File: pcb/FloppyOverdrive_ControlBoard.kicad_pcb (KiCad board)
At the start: 2 copper layers, 163 x 104 mm, 46 parts, among them J1 174804-1, J2 Motor_Header, J3 Bus_Connector, J4 Sensor_Header, J5 Heads_Header, J6 Step_Header, J7 PIC_ADC_Header, J8 FPGA_IO_Header, J9 HeadOut_Header, SW1 RST_Btn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

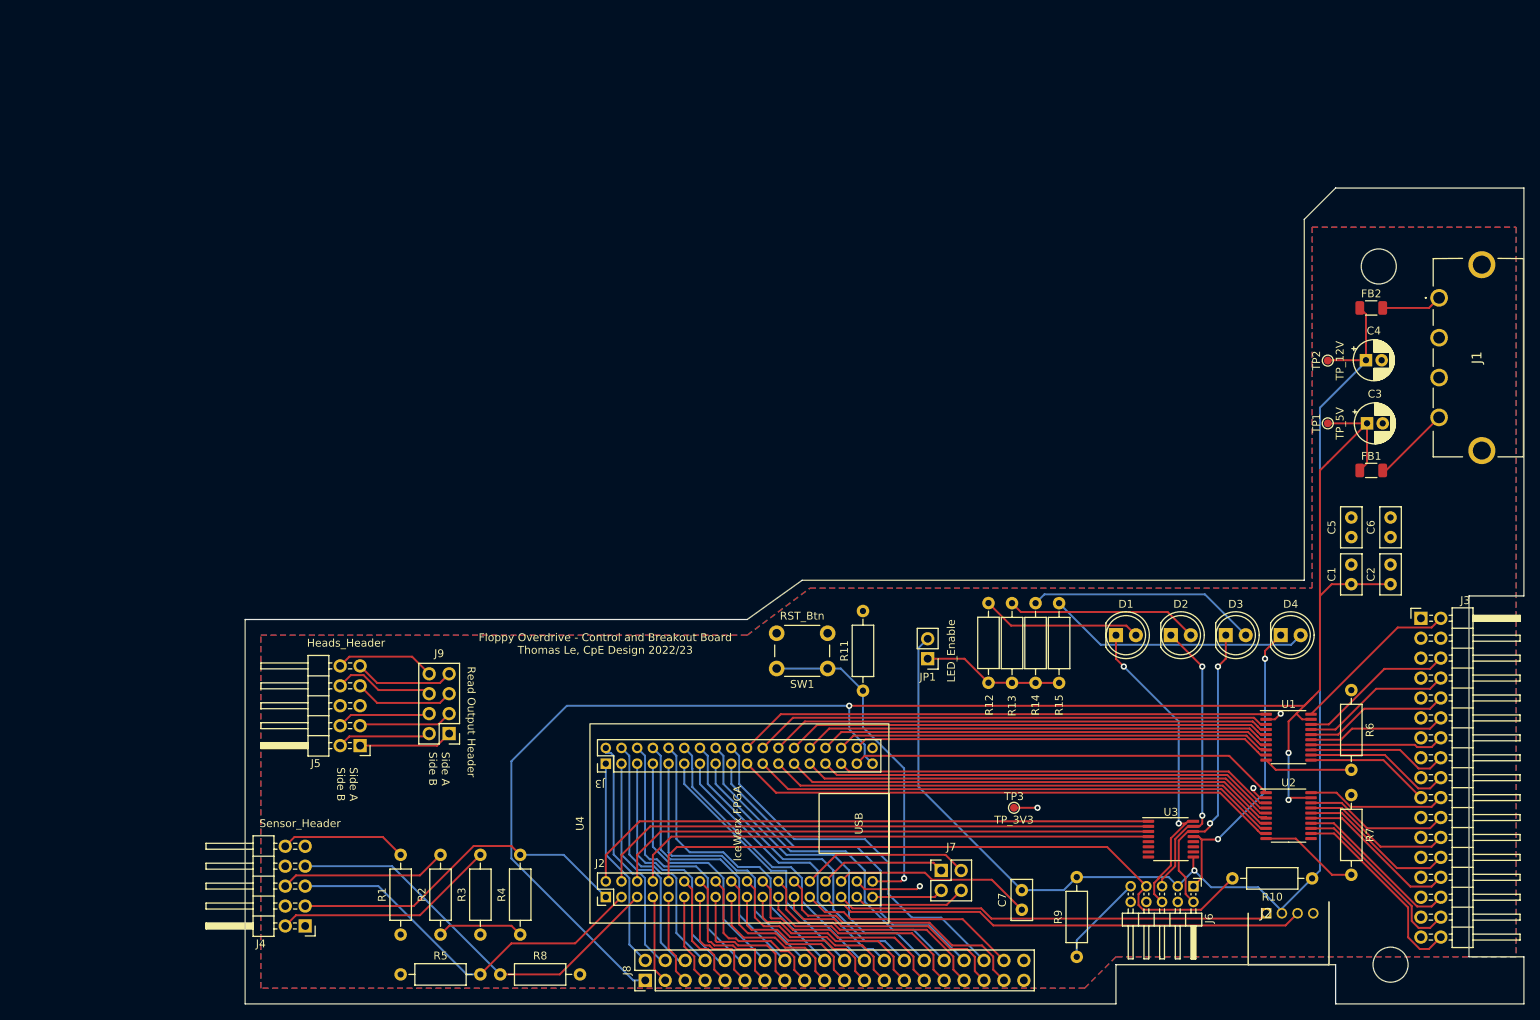
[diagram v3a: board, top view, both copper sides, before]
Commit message: Fixed incorrect routing, added silkscreen info
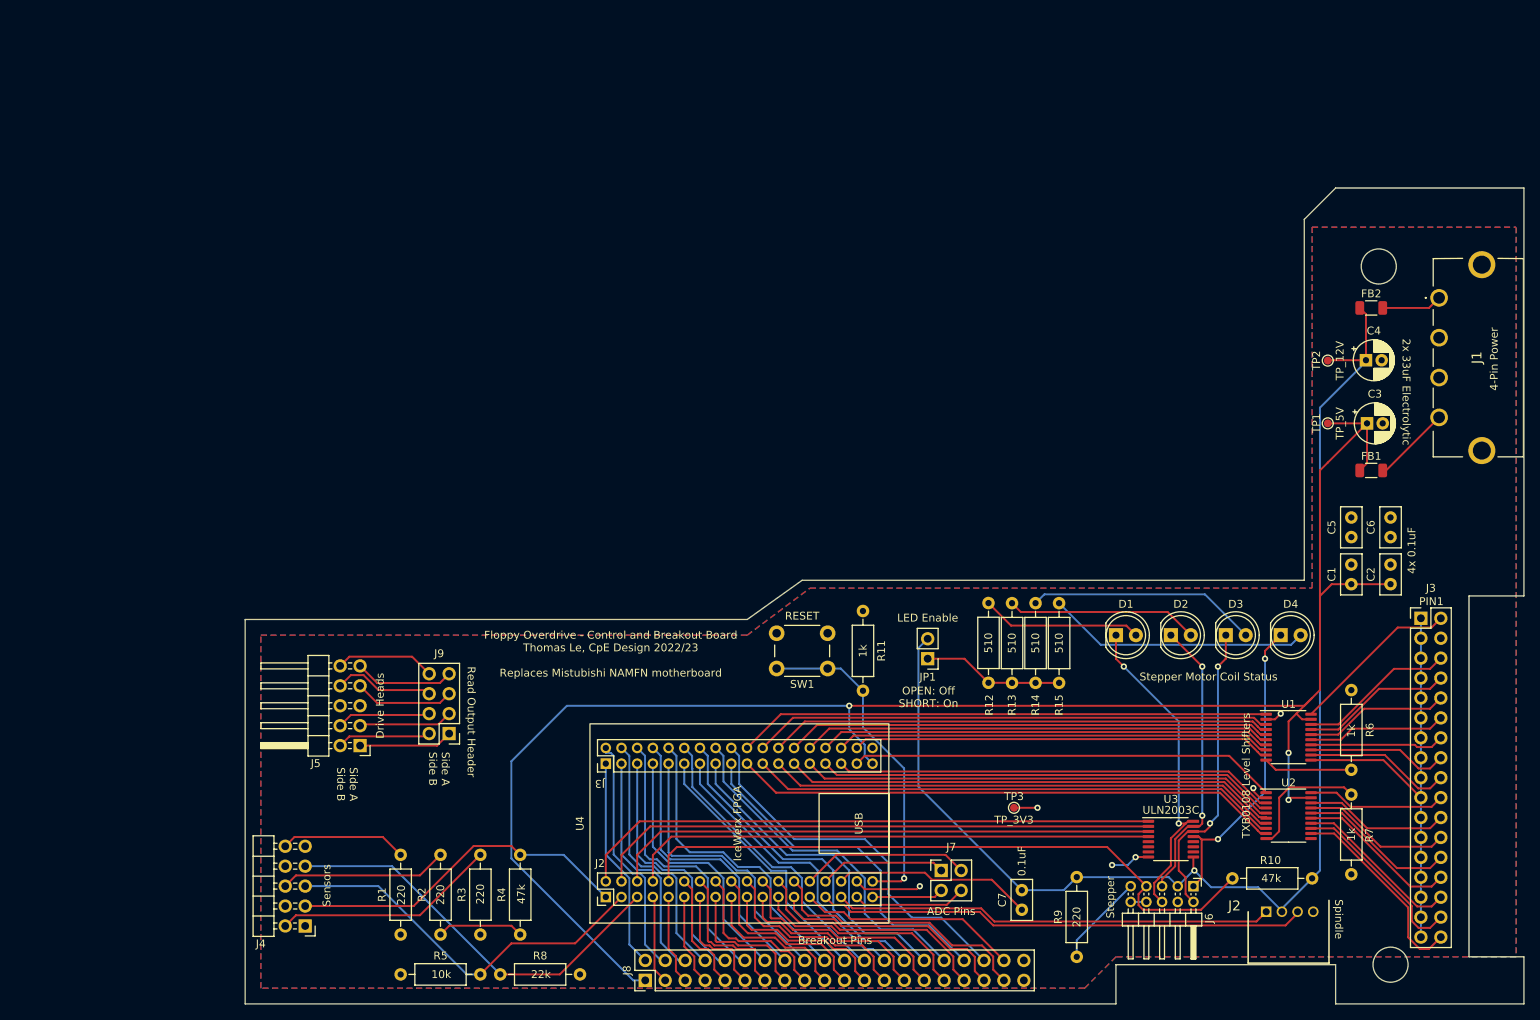
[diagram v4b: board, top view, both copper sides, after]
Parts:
- J3: footprint Connector_PinHeader_2.54mm:PinHeader_2x17_P2.54mm_Horizontal -> Connector_PinHeader_2.54mm:PinHeader_2x17_P2.54mm_Vertical
- J4: value Sensor_Header -> Sensors
- J5: value Heads_Header -> Drive Heads
- JP1: value LED_Enable -> LED Enable
- SW1: value RST_Btn -> RESET
- moved R7 10.1 mm to (205.0, 129.5), turned to 90 degrees
- moved J2 0.20 mm to (194.2, 134.2)
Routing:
- net GND: track 41.4 -> 89.1 mm, vias 0 -> 2
- net Net-(R7-Pad2): track 12.8 -> 16.5 mm
- net PIN_32: track 45.5 -> 44.9 mm
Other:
- board text added: "0.1uF"
- board text added: "10k"
- board text added: "1k"
- board text added: "220"
- board text added: "22k"
- board text added: "2x 33uF Electrolytic"
- board text added: "4-Pin Power"
- board text added: "47k"
- board text added: "4x 0.1uF"
- board text added: "510"
- board text added: "ADC Pins"
- board text added: "Breakout Pins"
- board text added: "Floppy Overdrive - Control and Breakout Board Thomas Le, CpE Design 2022/23 Replaces Mistubishi NAMFN motherboard"
- board text added: "OPEN: Off SHORT: On"
- board text added: "PIN1"
- board text added: "Spindle"
- board text added: "Stepper"
- board text added: "Stepper Motor Coil Status"
- board text added: "TXB0108 Level Shifters"
- board text added: "ULN2003C"
- board text removed: "Floppy Overdrive - Control and Breakout Board Thomas Le, CpE Design 2022/23"

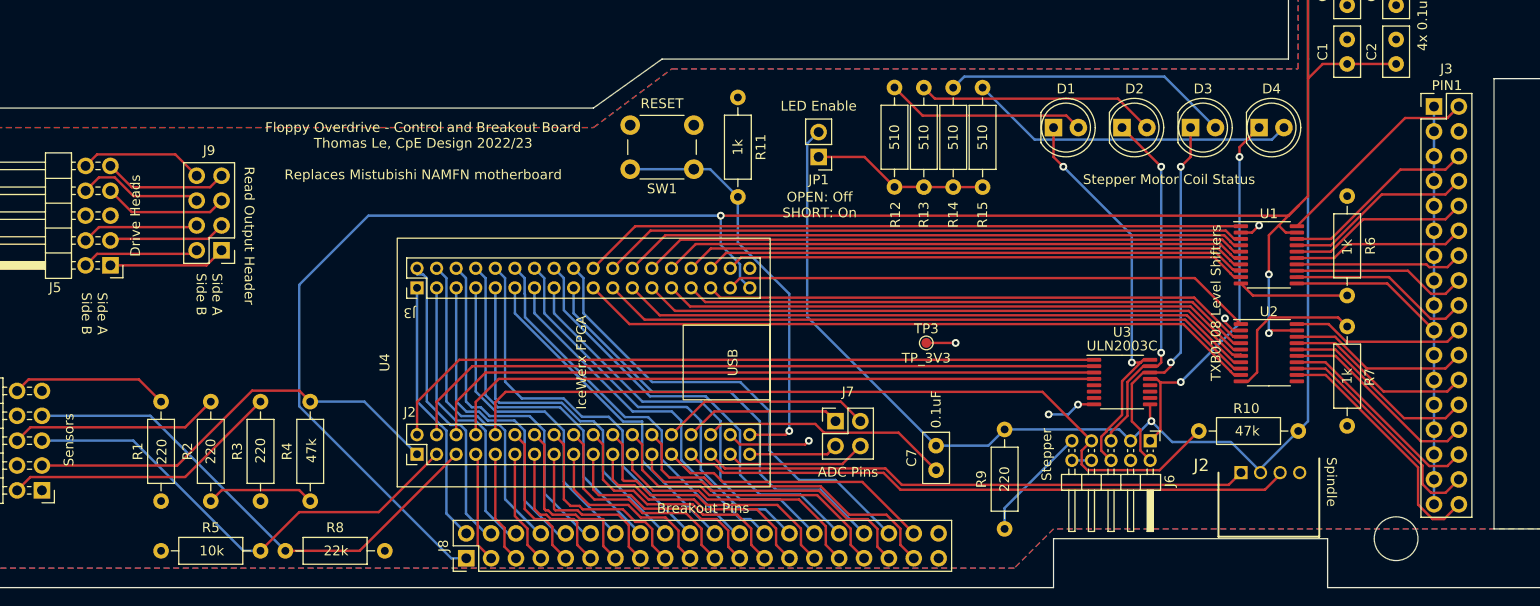
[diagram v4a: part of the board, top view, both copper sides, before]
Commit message: Fixed floppy bus orientation
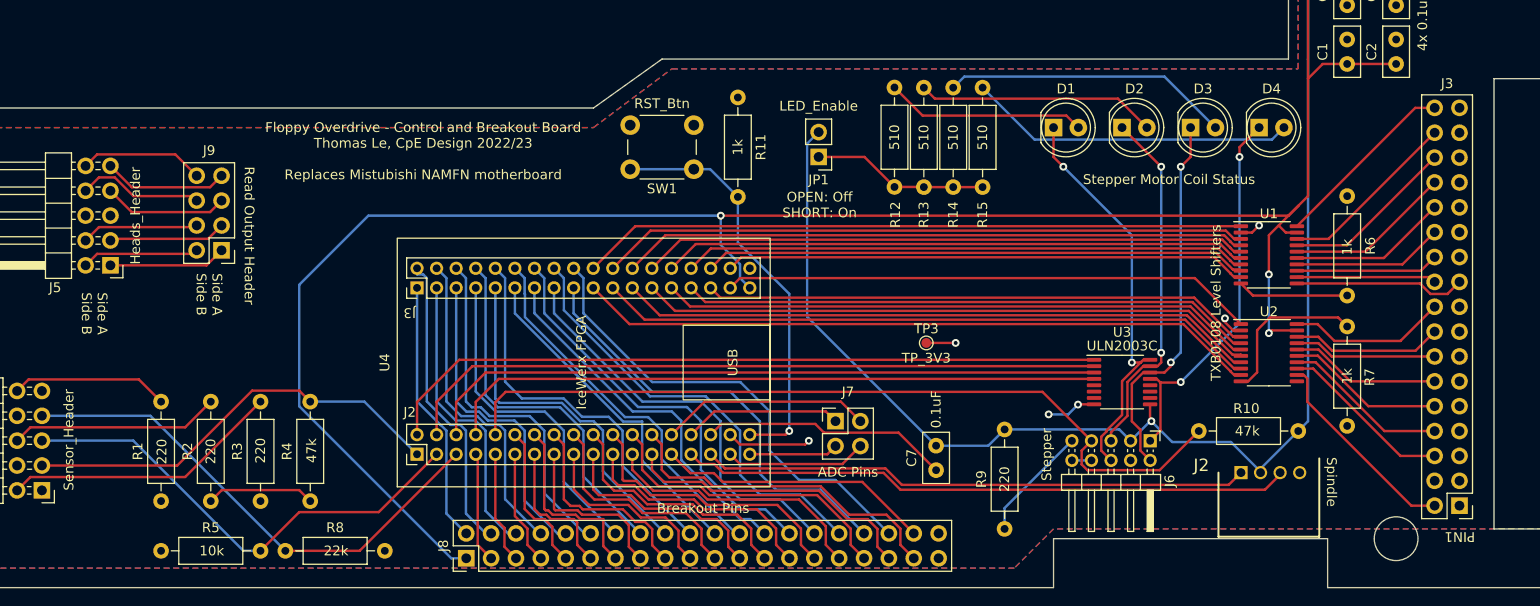
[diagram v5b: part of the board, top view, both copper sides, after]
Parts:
- J3: value Bus_Connector -> Floppy_Bus
- J4: value Sensors -> Sensor_Header
- J5: value Drive Heads -> Heads_Header
- JP1: value LED Enable -> LED_Enable
- SW1: value RESET -> RST_Btn
- moved J3 40.9 mm to (216.5, 137.6), turned to 180 degrees
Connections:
- J3 pad 10: Net-(J3-Pad10) -> Net-(U2-Pad15)
- J3 pad 12: Net-(J3-Pad12) -> Net-(U2-Pad16)
- J3 pad 14: Net-(J3-Pad14) -> Net-(U2-Pad17)
- J3 pad 16: Net-(J3-Pad16) -> Net-(U2-Pad18)
- J3 pad 18: Net-(J3-Pad18) -> Net-(U2-Pad20)
- J3 pad 2: Net-(J3-Pad2) -> Net-(U2-Pad12)
- J3 pad 20: Net-(J3-Pad20) -> Net-(U1-Pad12)
- J3 pad 22: Net-(J3-Pad22) -> Net-(U1-Pad13)
- J3 pad 24: Net-(J3-Pad24) -> Net-(U1-Pad14)
- J3 pad 26: Net-(J3-Pad26) -> Net-(U1-Pad15)
- J3 pad 28: Net-(J3-Pad28) -> Net-(U1-Pad16)
- J3 pad 30: Net-(J3-Pad30) -> Net-(U1-Pad17)
- J3 pad 32: Net-(J3-Pad32) -> Net-(U1-Pad18)
- J3 pad 34: Net-(J3-Pad34) -> Net-(U1-Pad20)
- J3 pad 6: Net-(J3-Pad6) -> Net-(U2-Pad13)
- J3 pad 8: Net-(J3-Pad8) -> Net-(U2-Pad14)
- U1 pad 1: Density -> Ready
- U1 pad 12: Net-(J3-Pad18) -> Net-(U1-Pad12)
- U1 pad 13: Net-(J3-Pad16) -> Net-(U1-Pad13)
- U1 pad 14: Net-(J3-Pad14) -> Net-(U1-Pad14)
- U1 pad 15: Net-(J3-Pad12) -> Net-(U1-Pad15)
- U1 pad 16: Net-(J3-Pad10) -> Net-(U1-Pad16)
- U1 pad 17: Net-(J3-Pad8) -> Net-(U1-Pad17)
- U1 pad 18: Net-(J3-Pad6) -> Net-(U1-Pad18)
- U1 pad 20: Net-(J3-Pad2) -> Net-(U1-Pad20)
- U1 pad 3: DriveSel_3 -> SideSel
- U1 pad 4: Index -> ReadData
- U1 pad 5: DriveSel_0 -> WriteProtect
- U1 pad 6: DriveSel_1 -> Track0
- U1 pad 7: DriveSel_2 -> WriteGate
- U1 pad 8: Motor -> WriteData
- U1 pad 9: StepDir -> Step
- U2 pad 1: Step -> StepDir
- U2 pad 12: Net-(J3-Pad34) -> Net-(U2-Pad12)
- U2 pad 13: Net-(J3-Pad32) -> Net-(U2-Pad13)
- U2 pad 14: Net-(J3-Pad30) -> Net-(U2-Pad14)
- U2 pad 15: Net-(J3-Pad28) -> Net-(U2-Pad15)
- U2 pad 16: Net-(J3-Pad26) -> Net-(U2-Pad16)
- U2 pad 17: Net-(J3-Pad24) -> Net-(U2-Pad17)
- U2 pad 18: Net-(J3-Pad22) -> Net-(U2-Pad18)
- U2 pad 20: Net-(J3-Pad20) -> Net-(U2-Pad20)
- U2 pad 3: WriteData -> Motor
- U2 pad 4: WriteGate -> DriveSel_2
- U2 pad 5: Track0 -> DriveSel_1
- U2 pad 6: WriteProtect -> DriveSel_0
- U2 pad 7: ReadData -> Index
- U2 pad 8: SideSel -> DriveSel_3
- U2 pad 9: Ready -> Density
- U4 pad J3.19: Ready -> Density
- U4 pad J3.20: Density -> Ready
- U4 pad J3.21: SideSel -> DriveSel_3
- U4 pad J3.22: DriveSel_3 -> SideSel
- U4 pad J3.23: ReadData -> Index
- U4 pad J3.24: Index -> ReadData
- U4 pad J3.25: WriteProtect -> DriveSel_0
- U4 pad J3.26: DriveSel_0 -> WriteProtect
- U4 pad J3.27: Track0 -> DriveSel_1
- U4 pad J3.28: DriveSel_1 -> Track0
- U4 pad J3.29: WriteGate -> DriveSel_2
- U4 pad J3.30: DriveSel_2 -> WriteGate
- U4 pad J3.31: WriteData -> Motor
- U4 pad J3.32: Motor -> WriteData
- U4 pad J3.33: Step -> StepDir
- U4 pad J3.34: StepDir -> Step
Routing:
- net GND: track 89.1 -> 50.1 mm
- net Net-(J3-Pad34): track 25.5 -> 0.00 mm
- net Net-(J3-Pad32): track 23.5 -> 0.00 mm
- net Net-(J3-Pad2): track 21.6 -> 0.00 mm
- net Net-(J3-Pad30): track 21.4 -> 0.00 mm
- net Net-(U2-Pad12): track 0.00 -> 21.0 mm
- net Net-(J3-Pad28): track 20.6 -> 0.00 mm
- net Net-(J3-Pad6): track 20.0 -> 0.00 mm
- net Net-(J3-Pad26): track 20.0 -> 0.00 mm
- net Net-(J3-Pad8): track 19.3 -> 0.00 mm
- net Net-(U1-Pad20): track 0.00 -> 19.1 mm
- net Net-(J3-Pad24): track 19.1 -> 0.00 mm
- net Net-(J3-Pad18): track 18.9 -> 0.00 mm
- net Net-(U1-Pad18): track 0.00 -> 18.6 mm
- net Net-(J3-Pad10): track 18.5 -> 0.00 mm
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
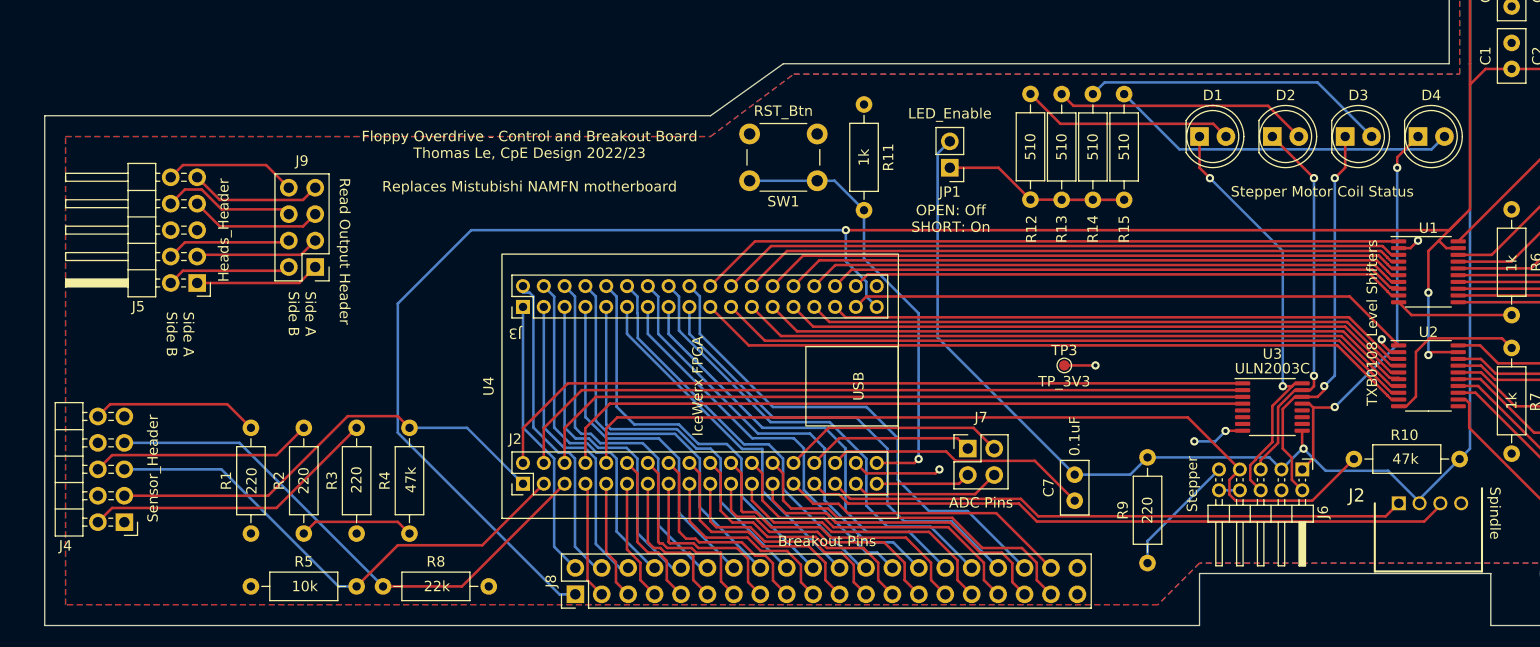
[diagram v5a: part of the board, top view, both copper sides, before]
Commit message: Added PCB test points, fixed schematic
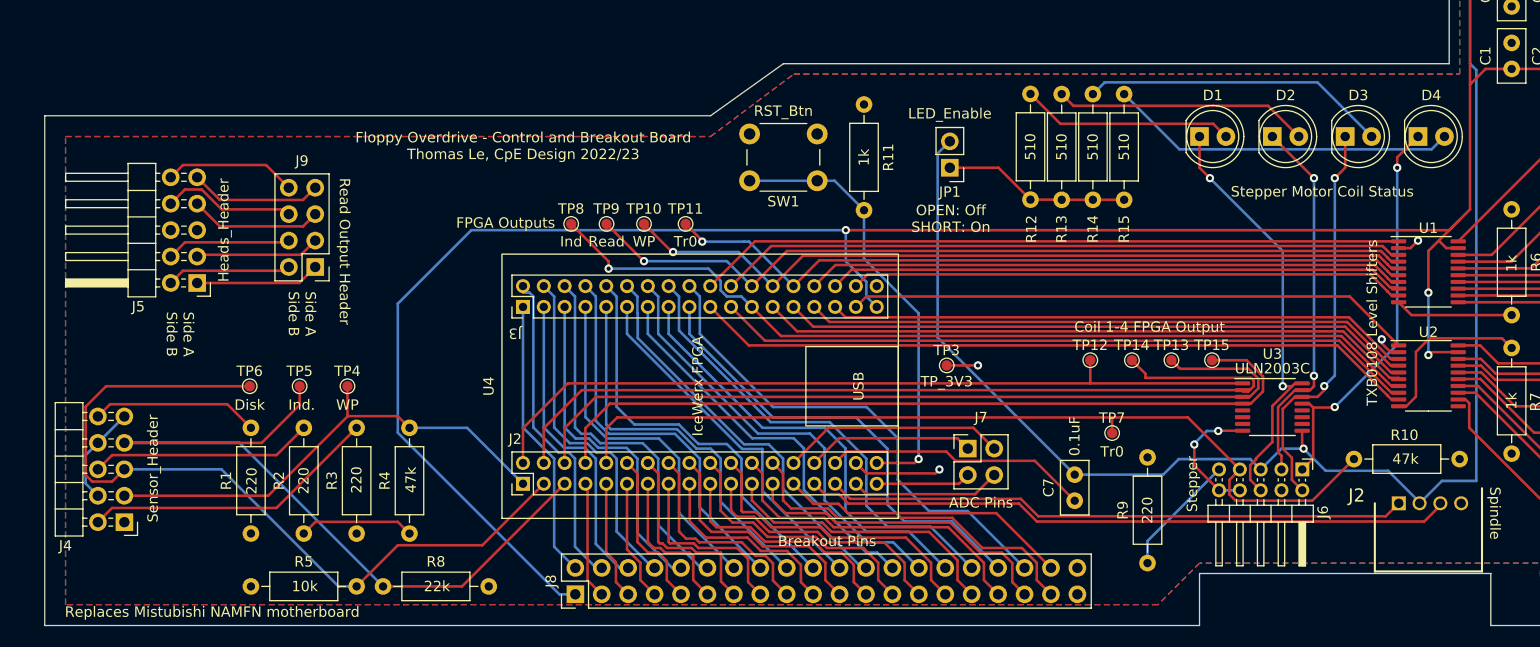
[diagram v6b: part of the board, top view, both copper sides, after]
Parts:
- added TP10: TP_WP5V, TestPoint:TestPoint_Pad_D1.0mm, F.Cu at (121.6, 107.4)
- added TP11: TP_Track05V, TestPoint:TestPoint_Pad_D1.0mm, F.Cu at (125.6, 107.4)
- added TP12: TP_Coil1, TestPoint:TestPoint_Pad_D1.0mm, F.Cu at (164.5, 120.5)
- added TP13: TP_Coil3, TestPoint:TestPoint_Pad_D1.0mm, F.Cu at (172.3, 120.5)
- added TP14: TP_Coil2, TestPoint:TestPoint_Pad_D1.0mm, F.Cu at (168.5, 120.5)
- added TP15: TP_Coil4, TestPoint:TestPoint_Pad_D1.0mm, F.Cu at (176.2, 120.5)
- added TP4: TP_WP, TestPoint:TestPoint_Pad_D1.0mm, F.Cu at (93.1, 123.0)
- added TP5: TP_Index, TestPoint:TestPoint_Pad_D1.0mm, F.Cu at (88.5, 123.0)
- added TP6: TP_Disk, TestPoint:TestPoint_Pad_D1.0mm, F.Cu at (83.7, 123.0)
- added TP7: TP_Track0, TestPoint:TestPoint_Pad_D1.0mm, F.Cu at (166.6, 127.5)
- added TP8: TP_Index5V, TestPoint:TestPoint_Pad_D1.0mm, F.Cu at (114.6, 107.4)
- added TP9: TP_Read5V, TestPoint:TestPoint_Pad_D1.0mm, F.Cu at (118.0, 107.4)
- moved TP3 11.3 mm to (150.7, 121.0)
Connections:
- J6 pad a2: +12V -> C2_Mot
- J6 pad a3: C2_Mot -> +12V
- R10 pad 1: +12V -> +3V3
- R9 pad 2: +12V -> +3V3
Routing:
- net Disk_Sens: track 49.1 -> 76.7 mm
- net Index: track 65.3 -> 86.9 mm, vias 0 -> 1
- net Index_Sens: track 52.1 -> 72.3 mm
- net ReadData: track 64.0 -> 80.4 mm, vias 0 -> 1
- net GND: track 50.1 -> 65.3 mm
- net WriteProtect: track 61.9 -> 76.7 mm, vias 0 -> 1
- net Coil_2: track 72.0 -> 86.7 mm
- net Track0: track 59.8 -> 72.7 mm, vias 0 -> 1
- net Coil_3: track 69.8 -> 81.6 mm
- net Coil_4: track 67.5 -> 76.9 mm
- net WP_Sens: track 44.2 -> 47.1 mm
- net +12V: track 164.2 -> 166.9 mm
- net Coil_1: track 74.3 -> 76.5 mm
- net Track0_Sens: track 83.4 -> 84.9 mm
- net C2_Mot: track 36.5 -> 36.0 mm
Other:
- board text added: "Coil 1-4 FPGA Output"
- board text added: "Disk"
- board text added: "FPGA Outputs"
- board text added: "Floppy Overdrive - Control and Breakout Board Thomas Le, CpE Design 2022/23"
- board text added: "Ind"
- board text added: "Ind."
- board text added: "Read"
- board text added: "Replaces Mistubishi NAMFN motherboard"
- board text added: "Tr0"
- board text added: "WP"
- board text removed: "Floppy Overdrive - Control and Breakout Board Thomas Le, CpE Design 2022/23 Replaces Mistubishi NAMFN motherboard"

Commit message: Sync backups
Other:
- board text added: "2"
- board text added: "34"
- board text added: "P1"
- board text removed: "PIN1"
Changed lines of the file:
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@@
     (effects (font (size 1 1) (thickness 0.15)))
   )
-  (gr_text "PIN1" (at 216.5 140.8 180) (layer "F.SilkS")
+  (gr_text "P1" (at 216.5 140.8 180) (layer "F.SilkS")
     (effects (font (size 1 1) (thickness 0.15)))
   )
@@
   )
   (gr_text "510" (at 161.75 100 90) (layer "F.SilkS")
+    (effects (font (size 1 1) (thickness 0.15)))
+  )
+  (gr_text "2" (at 213.9 140.8 180) (layer "F.SilkS")
     (effects (font (size 1 1) (thickness 0.15)))
   )
@@
     (effects (font (size 1 1) (thickness 0.15)))
   )
+  (gr_text "34" (at 211.4 96.9 90) (layer "F.SilkS")
+    (effects (font (size 1 1) (thickness 0.15)))
+  )
